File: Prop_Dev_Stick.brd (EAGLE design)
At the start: 63.2 x 24.9 mm, 54 parts, among them J1 10118193-0001LF, J3 M20-7822046, J4 M20-7822046, J5 M20-7820442, J6 M20-7820442, U1 P8X32A-Q44, U2 FT230XQ-R, U3 TPS2113ADRBR, U4 CAT24C512WI-GT3, U5 AD7999YRJZ-1500RL7, U6 TS2937CW33, U7 IRLML6401TRPBF, X1 ATS060CSM-1

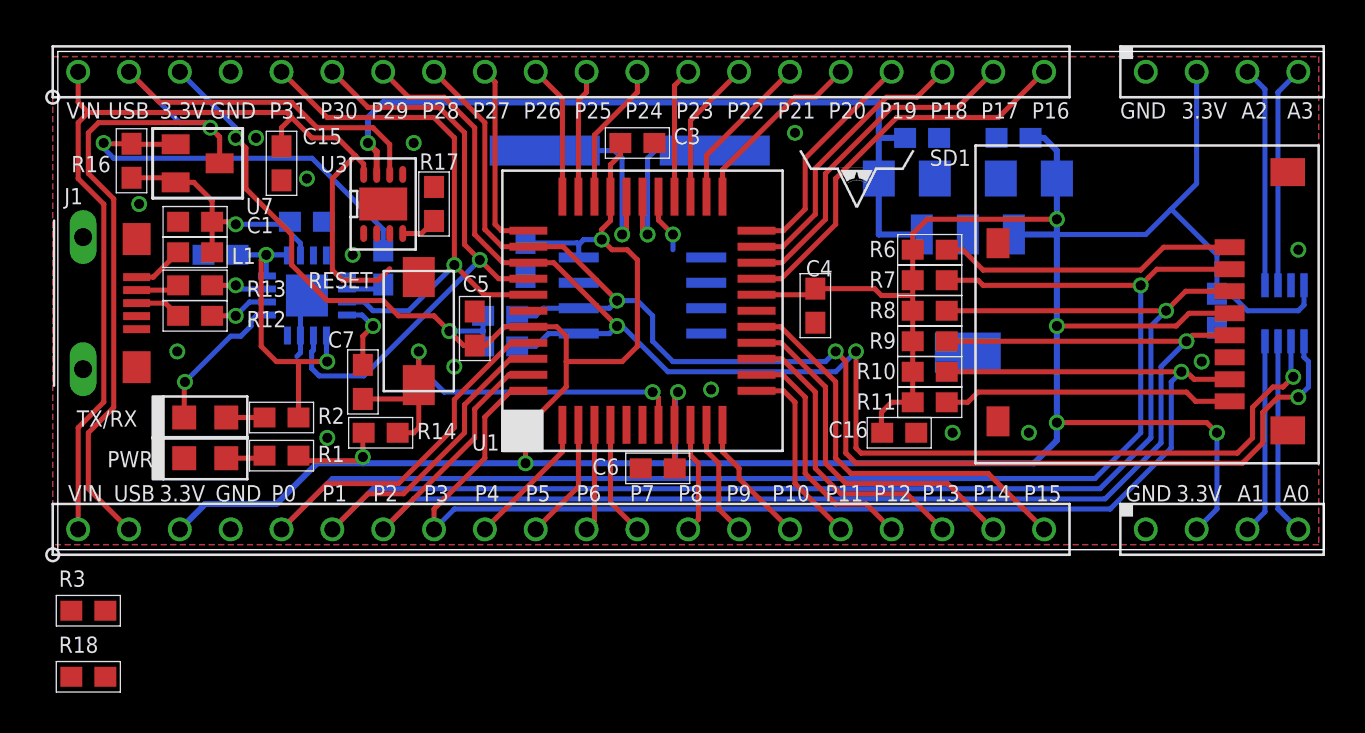
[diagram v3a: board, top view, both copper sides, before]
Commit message: Changed SD Card Slot.
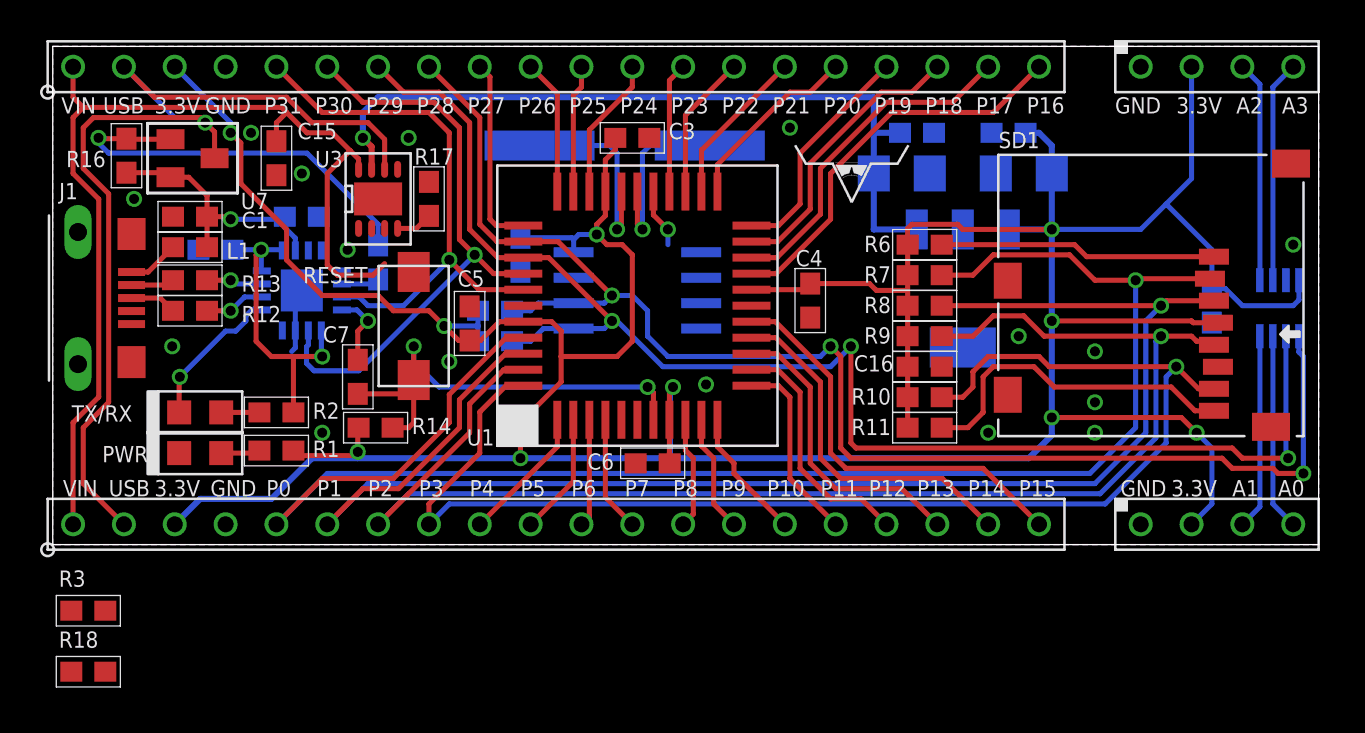
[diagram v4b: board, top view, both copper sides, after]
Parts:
- SD1: value 502570-0893 -> MF-CON-MICROSDSLOT-RIGHT; device PP_Connectors:502570-0893 -> MF_Connectors:MICROSDSLOT-RIGHT
- moved SD1 4.62 mm to (54.9, 12.4)
- moved C16 3.54 mm to (43.6, 8.89)
- moved R11 1.30 mm to (43.6, 5.84)
- moved R10 1.30 mm to (43.6, 7.37)
- moved J5 0.36 mm to (58.2, 23.9)
- moved U$2 0.36 mm to (41.9, 17.0)
- moved J6 0.36 mm to (58.2, 1.02)
- moved C4 0.36 mm to (37.8, 12.2)
- moved C3 0.36 mm to (29.0, 20.3)
- moved RESET 0.36 mm to (18.0, 10.9)
- moved X1 0.36 mm to (28.6, 19.9)
- moved J1 0.36 mm to (1.40, 12.3)
- moved R16 0.36 mm to (3.68, 19.4)
- moved PWR 0.36 mm to (7.37, 4.57)
- moved TX/RX 0.36 mm to (7.37, 6.60)
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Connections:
- net 3.3V: now also SD1.PIN4; no longer SD1.5
- net GND: now also SD1.G0, SD1.G1, SD1.PIN6; no longer SD1.3, SD1.SHIELD0, SD1.SHIELD1, SD1.SHIELD2, SD1.SHIELD3
- net IRQ: now also SD1.PIN8; no longer SD1.1
- net RW: now also SD1.PIN1; no longer SD1.8
- net SD_CS: now also SD1.PIN2; no longer SD1.7
- net SD_DI: now also SD1.PIN3; no longer SD1.6
- net SD_DO: now also SD1.PIN7; no longer SD1.2
- net SD_SCLK: now also SD1.PIN5; no longer SD1.4
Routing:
- net 3.3V: track 208.6 -> 206.0 mm
- net SCL: track 68.9 -> 71.3 mm
- net IRQ: track 14.5 -> 16.8 mm
- net SDA: track 69.9 -> 71.9 mm
- net SD_DO: track 66.2 -> 67.5 mm
- net RW: track 15.0 -> 13.9 mm
- net SD_DI: track 78.1 -> 77.3 mm
- net GND: vias 15 -> 17

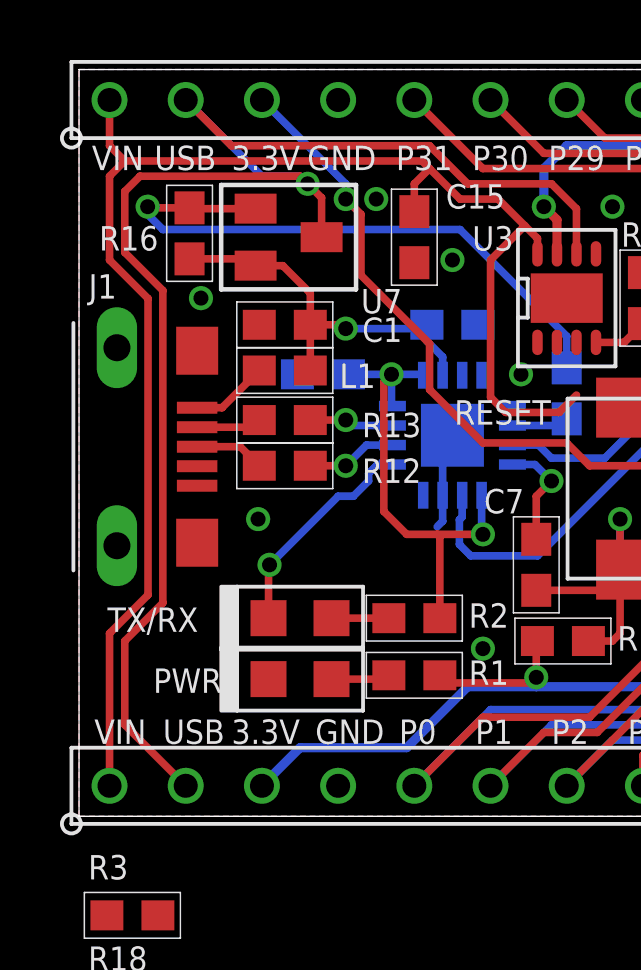
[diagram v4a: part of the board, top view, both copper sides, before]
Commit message: Changed USB connector
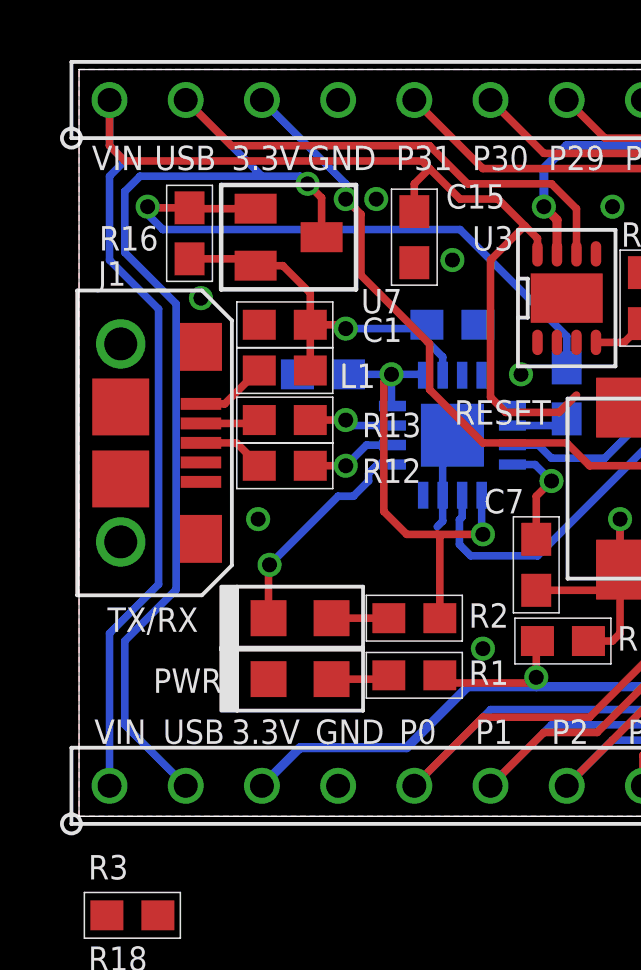
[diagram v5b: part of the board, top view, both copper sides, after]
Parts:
- J1: value 10118193-0001LF -> MF-CON-MICROUSB-RIGHT; device PP_Connectors:10118193-0001LF -> MF_Connectors:MICROUSB-RIGHT
- moved J1 1.40 mm to (2.79, 12.4)
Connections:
- net GND: now also J1.S5, J1.S6
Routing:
- net VIN: track 50.8 -> 53.4 mm
- net VBUS_P2: track 51.3 -> 50.1 mm
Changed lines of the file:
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@@
 <attribute name="NAME" x="21.879" y="17.0815" size="0.8128" layer="26" font="vector" rot="MR180"/>
-</element>
-<element name="J1" library="PP_Connectors" package="10118193-0001LF" value="10118193-0001LF" x="1.397" y="12.319" smashed="yes" rot="R270">
-<attribute name="NAME" x="0.318" y="17.256" size="0.8128" layer="25" font="vector"/>
 </element>
 <element name="R6" library="PP_Passives" package="0603" value="10K" x="43.561" y="14.986" smashed="yes" rot="R180">
@@
 <element name="SD1" library="MF_Connectors" package="MICROSDSLOT-RIGHT" value="MF-CON-MICROSDSLOT-RIGHT" x="54.864" y="12.446" smashed="yes" rot="R270">
 <attribute name="NAME" x="47.25225" y="19.807" size="0.8128" layer="21" font="vector"/>
+</element>
+<element name="J1" library="MF_Connectors" package="MICROUSB-RIGHT" value="MF-CON-MICROUSB-RIGHT" x="2.794" y="12.446" smashed="yes" rot="R270">
+<attribute name="NAME" x="0.635" y="17.686" size="0.8128" layer="25" font="vector"/>
 </element>
 </elements>
@@
 <contactref element="U1" pad="39"/>
 <contactref element="U1" pad="6"/>
-<contactref element="J1" pad="5"/>
-<contactref element="J1" pad="S1"/>
-<contactref element="J1" pad="S2"/>
-<contactref element="J1" pad="S3"/>
-<contactref element="J1" pad="S4"/>
 <contactref element="C1" pad="2"/>
 <contactref element="U2" pad="3"/>
@@
 <via x="52.07" y="7.112" extent="1-16" drill="0.5"/>
 <via x="52.07" y="5.588" extent="1-16" drill="0.5"/>
+<contactref element="J1" pad="5"/>
+<contactref element="J1" pad="5"/>
+<contactref element="J1" pad="S1"/>
+<contactref element="J1" pad="S4"/>
+<contactref element="J1" pad="S5"/>
+<contactref element="J1" pad="S6"/>
+<contactref element="J1" pad="S3"/>
+<contactref element="J1" pad="S2"/>
+<wire x1="8.636" y1="1.016" x2="0.928" y2="-6.35" width="0" layer="19" extent="1-1"/>
 </signal>
 <signal name="SDA">
@@
 </signal>
 <signal name="VBUS">
+<contactref element="L1" pad="1"/>
 <contactref element="J1" pad="1"/>
-<contactref element="L1" pad="1"/>
-<wire x1="3.937" y1="13.619" x2="4.768" y2="13.619" width="0.254" layer="1"/>
-<wire x1="4.768" y1="13.619" x2="6.008" y2="14.859" width="0.254" layer="1"/>
+<wire x1="4.064" y1="13.746" x2="4.856" y2="13.746" width="0.254" layer="1"/>
+<wire x1="4.856" y1="13.746" x2="5.969" y2="14.859" width="0.254" layer="1"/>
+<wire x1="5.969" y1="14.859" x2="6.008" y2="14.859" width="0.254" layer="1"/>
 </signal>
 <signal name="D+">
+<contactref element="R12" pad="2"/>
+<wire x1="5.246" y1="12.446" x2="6.008" y2="11.684" width="0.254" layer="1"/>
 <contactref element="J1" pad="3"/>
-<contactref element="R12" pad="2"/>
-<wire x1="3.937" y1="12.319" x2="5.373" y2="12.319" width="0.254" layer="1"/>
-<wire x1="5.373" y1="12.319" x2="6.008" y2="11.684" width="0.254" layer="1"/>
+<wire x1="4.064" y1="12.446" x2="5.246" y2="12.446" width="0.254" layer="1"/>
 </signal>
 <signal name="RX">
@@
 </signal>
 <signal name="D-">
+<contactref element="R13" pad="2"/>
+<wire x1="6.008" y1="12.969" x2="6.008" y2="13.208" width="0.254" layer="1"/>
 <contactref element="J1" pad="2"/>
-<contactref element="R13" pad="2"/>
-<wire x1="3.937" y1="12.969" x2="6.008" y2="12.969" width="0.254" layer="1"/>
-<wire x1="6.008" y1="12.969" x2="6.008" y2="13.208" width="0.254" layer="1"/>
+<wire x1="4.064" y1="13.096" x2="5.896" y2="13.096" width="0.254" layer="1"/>
+<wire x1="5.896" y1="13.096" x2="6.008" y2="13.208" width="0.254" layer="1"/>
 </signal>
 <signal name="5V">
@@
 <wire x1="16.581" y1="20.249" x2="16.581" y2="18.747" width="0.254" layer="1"/>
 <wire x1="6.096" y1="21.336" x2="3.556" y2="23.876" width="0.254" layer="16"/>
-<wire x1="3.556" y1="1.016" x2="1.524" y2="3.048" width="0.254" layer="1"/>
-<wire x1="1.524" y1="3.048" x2="1.524" y2="5.842" width="0.254" layer="1"/>
-<wire x1="1.524" y1="5.842" x2="2.794" y2="7.112" width="0.254" layer="1"/>
-<wire x1="2.794" y1="7.112" x2="2.794" y2="17.526" width="0.254" layer="1"/>
-<wire x1="2.794" y1="17.526" x2="1.524" y2="18.796" width="0.254" layer="1"/>
-<wire x1="1.524" y1="18.796" x2="1.524" y2="20.828" width="0.254" layer="1"/>
-<wire x1="1.524" y1="20.828" x2="2.032" y2="21.336" width="0.254" layer="1"/>
+<wire x1="3.556" y1="1.016" x2="1.524" y2="3.048" width="0.254" layer="16"/>
+<wire x1="1.524" y1="3.048" x2="1.524" y2="5.842" width="0.254" layer="16"/>
+<wire x1="1.524" y1="5.842" x2="3.233846875" y2="7.551846875" width="0.254" layer="16"/>
+<wire x1="3.233846875" y1="7.551846875" x2="3.233846875" y2="17.086153125" width="0.254" layer="16"/>
+<wire x1="3.233846875" y1="17.086153125" x2="1.524" y2="18.796" width="0.254" layer="16"/>
+<wire x1="1.524" y1="18.796" x2="1.524" y2="20.828" width="0.254" layer="16"/>
+<wire x1="1.524" y1="20.828" x2="2.032" y2="21.336" width="0.254" layer="16"/>
 <wire x1="8.085" y1="19.304" x2="8.085" y2="20.617" width="0.254" layer="1"/>
-<wire x1="7.62" y1="21.082" x2="7.366" y2="21.336" width="0.254" layer="1"/>
-<wire x1="7.366" y1="21.336" x2="2.032" y2="21.336" width="0.254" layer="1"/>
+<wire x1="6.096" y1="21.336" x2="2.032" y2="21.336" width="0.254" layer="16"/>
 <wire x1="6.096" y1="21.336" x2="7.366" y2="21.336" width="0.254" layer="16"/>
 <wire x1="7.366" y1="21.336" x2="7.62" y2="21.082" width="0.254" layer="16"/>
@@
 <wire x1="14.859" y1="19.685" x2="15.281" y2="19.263" width="0.254" layer="1"/>
 <wire x1="15.281" y1="19.263" x2="15.281" y2="18.747" width="0.254" layer="1"/>
-<wire x1="1.016" y1="1.016" x2="1.016" y2="6.096" width="0.254" layer="1"/>
-<wire x1="1.016" y1="6.096" x2="2.29904375" y2="7.37904375" width="0.254" layer="1"/>
-<wire x1="2.29904375" y1="7.37904375" x2="2.29904375" y2="17.25895625" width="0.254" layer="1"/>
-<wire x1="2.29904375" y1="17.25895625" x2="1.016" y2="18.542" width="0.254" layer="1"/>
-<wire x1="1.016" y1="23.876" x2="1.016" y2="22.352" width="0.254" layer="1"/>
-<wire x1="1.016" y1="22.352" x2="1.524" y2="21.844" width="0.254" layer="1"/>
-<wire x1="1.524" y1="21.844" x2="1.016" y2="21.336" width="0.254" layer="1"/>
-<wire x1="1.016" y1="21.336" x2="1.016" y2="18.542" width="0.254" layer="1"/>
+<wire x1="1.016" y1="1.016" x2="1.016" y2="6.096" width="0.254" layer="16"/>
+<wire x1="1.016" y1="6.096" x2="2.651153125" y2="7.731153125" width="0.254" layer="16"/>
+<wire x1="2.651153125" y1="7.731153125" x2="2.651153125" y2="16.906846875" width="0.254" layer="16"/>
+<wire x1="2.651153125" y1="16.906846875" x2="1.016" y2="18.542" width="0.254" layer="16"/>
+<wire x1="1.016" y1="23.876" x2="1.016" y2="22.352" width="0.254" layer="16"/>
+<wire x1="1.016" y1="22.352" x2="1.524" y2="21.844" width="0.254" layer="16"/>
+<wire x1="1.524" y1="21.844" x2="1.016" y2="21.336" width="0.254" layer="16"/>
+<wire x1="1.016" y1="21.336" x2="1.016" y2="18.542" width="0.254" layer="16"/>
 <wire x1="11.43" y1="21.844" x2="1.524" y2="21.844" width="0.254" layer="1"/>
 <wire x1="16.581" y1="14.041" x2="16.002" y2="13.462" width="0.254" layer="1"/>
@@
 <wire x1="11.176" y1="21.082" x2="11.684" y2="21.59" width="0.254" layer="1"/>
 <contactref element="R3" pad="2"/>
+<wire x1="1.524" y1="21.844" x2="1.016" y2="22.352" width="0.254" layer="1"/>
+<wire x1="1.016" y1="22.352" x2="1.016" y2="23.876" width="0.254" layer="1"/>
 <wire x1="2.628" y1="-3.302" x2="1.016" y2="1.016" width="0" layer="19" extent="1-1"/>
 </signal>
@@
 <contactref element="R3" pad="1"/>
 <contactref element="R18" pad="2"/>
-<wire x1="16.581" y1="15.797" x2="2.628" y2="-6.35" width="0" layer="19" extent="1-1"/>
 <wire x1="0.928" y1="-3.302" x2="16.581" y2="15.797" width="0" layer="19" extent="1-1"/>
+<wire x1="2.628" y1="-6.35" x2="0.928" y2="-3.302" width="0" layer="19" extent="1-1"/>
 </signal>
 </signals>

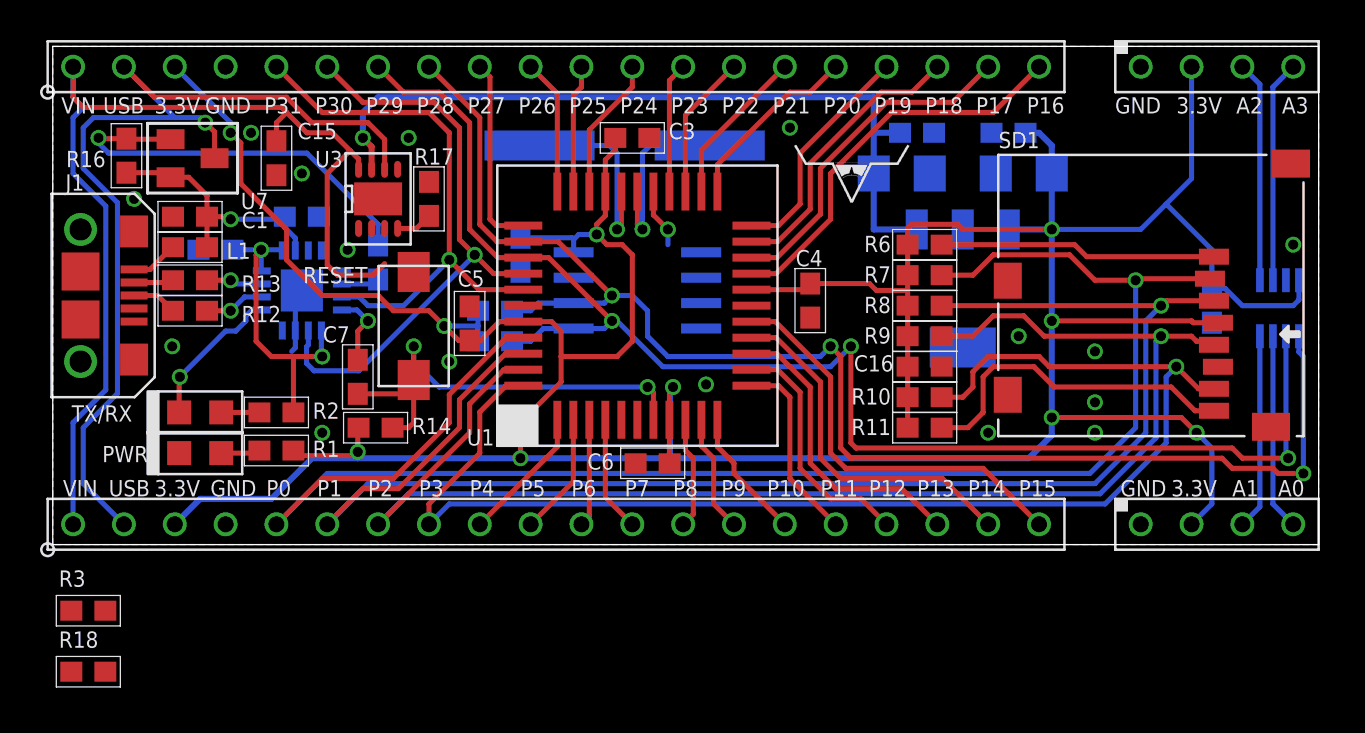
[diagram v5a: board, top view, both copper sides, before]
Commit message: Routed power switching for LDO dropout
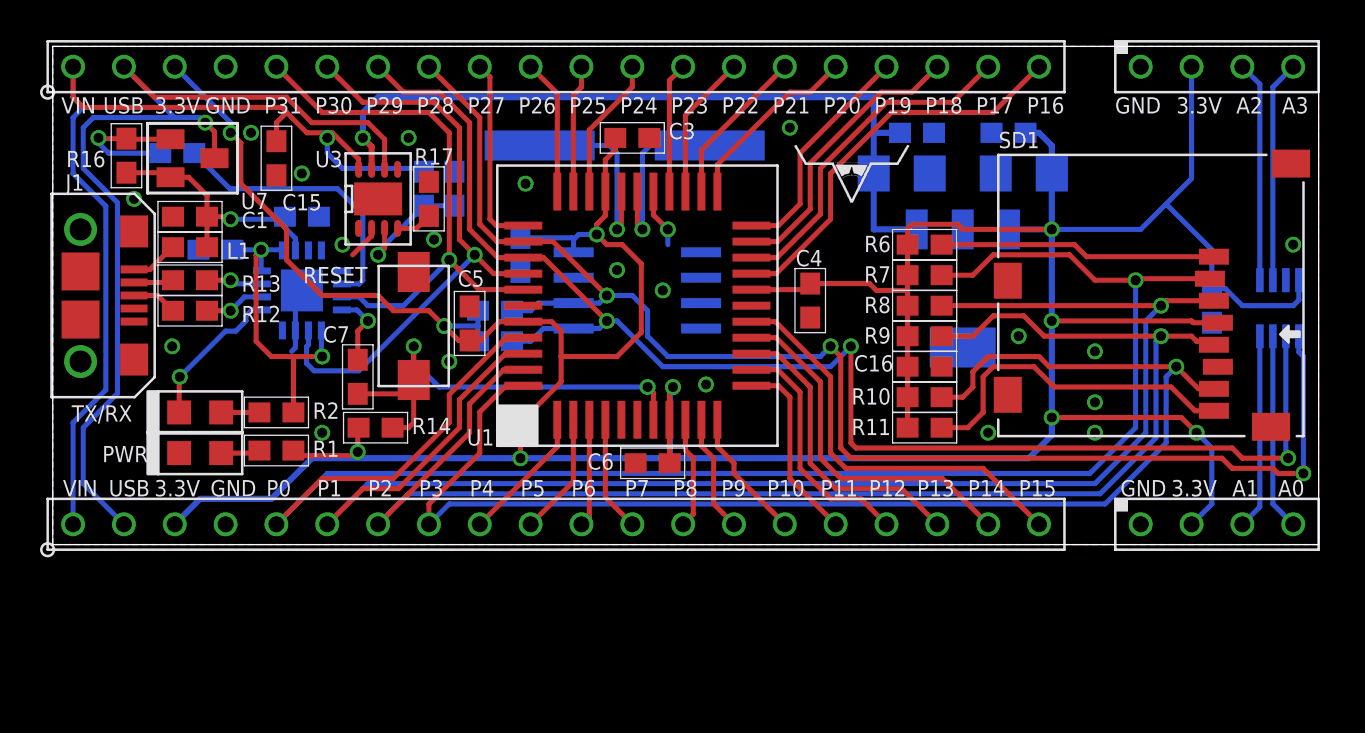
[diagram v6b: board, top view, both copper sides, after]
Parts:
- moved R18 30.3 mm to (20.1, 17.8), flipped to the bottom, turned to 270 degrees
- moved R3 26.9 mm to (18.5, 17.8), flipped to the bottom, turned to 90 degrees
- moved R15 11.4 mm to (6.22, 19.6), turned to 180 degrees
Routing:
- net N$41: track 20.6 -> 7.18 mm
- net PWREN: track 1.90 -> 14.1 mm
- net VSNS: track 0.00 -> 6.38 mm, vias 0 -> 1
- net VIN: track 53.4 -> 50.1 mm, vias 0 -> 1
- net GND: track 6.21 -> 7.92 mm, vias 17 -> 21
